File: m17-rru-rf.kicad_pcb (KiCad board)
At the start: 4 copper layers, 255 x 165 mm, 182 parts, among them J1 Conn_01x01_Pin, J2 Conn_Coaxial, J3 Conn_01x05, J4 Conn_01x05, J5 Conn_01x16, J6 Conn_Coaxial, Q1 BSS138, Q2 BSS138, Q3 NP100P04PDG, U1 LM317_SOT-223, U10 CC1200, U11 AD8318ACPZ-REEL7, U12 AD8318ACPZ-REEL7, U13 STM32F405RGTx, U2 LT1013DIDR, U3 TL431, U4 RA60H3847H1, U6 CC1200, X1 40MHz, Y1 12MHz

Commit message: LM317 protection diode location update
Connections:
- C3 pad 1: Net-(U1-ADJ) -> Net-(D2-A)
- D2 pad 2: GND -> Net-(D2-A)
- R6 pad 1: Net-(U1-ADJ) -> Net-(D2-A)
- R7 pad 2: Net-(U1-ADJ) -> Net-(D2-A)
- U1 pad 1: Net-(U1-ADJ) -> Net-(D2-A)
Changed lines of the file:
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@@
   (net 19 "Net-(U11-INHI)")
   (net 20 "Net-(R1-Pad2)")
-  (net 21 "Net-(U1-ADJ)")
+  (net 21 "Net-(D2-A)")
   (net 22 "Net-(U11-TADJ)")
   (net 23 "unconnected-(U11-TEMP-Pad13)")
@@
       (net 27 "Net-(R7-Pad1)") (pintype "passive"))
     (pad "2" smd roundrect (at 0.825 0) (size 0.8 0.95) (layers "F.Cu" "F.Paste" "F.Mask") (roundrect_rratio 0.25)
-      (net 21 "Net-(U1-ADJ)") (pintype "passive"))
+      (net 21 "Net-(D2-A)") (pintype "passive"))
     (model "${KICAD6_3DMODEL_DIR}/Resistor_SMD.3dshapes/R_0603_1608Metric.wrl"
       (offset (xyz 0 0 0))
@@
       (stroke (width 0.1) (type solid)) (layer "F.Fab"))
     (pad "1" smd roundrect (at -0.825 0) (size 0.8 0.95) (layers "F.Cu" "F.Paste" "F.Mask") (roundrect_rratio 0.25)
-      (net 21 "Net-(U1-ADJ)") (pintype "passive"))
+      (net 21 "Net-(D2-A)") (pintype "passive"))
     (pad "2" smd roundrect (at 0.825 0) (size 0.8 0.95) (layers "F.Cu" "F.Paste" "F.Mask") (roundrect_rratio 0.25)
       (net 24 "Net-(D1-A)") (pintype "passive"))
@@
       (stroke (width 0.1) (type solid)) (layer "F.Fab"))
     (pad "1" smd rect (at -3.15 -2.3) (size 2 1.5) (layers "F.Cu" "F.Paste" "F.Mask")
-      (net 21 "Net-(U1-ADJ)") (pinfunction "ADJ") (pintype "input"))
+      (net 21 "Net-(D2-A)") (pinfunction "ADJ") (pintype "input"))
     (pad "2" smd rect (at -3.15 0) (size 2 1.5) (layers "F.Cu" "F.Paste" "F.Mask")
       (net 24 "Net-(D1-A)") (pinfunction "VO") (pintype "power_out"))
@@
       (stroke (width 0.1) (type solid)) (layer "F.Fab"))
     (pad "1" smd roundrect (at -0.775 0) (size 0.9 0.95) (layers "F.Cu" "F.Paste" "F.Mask") (roundrect_rratio 0.25)
-      (net 21 "Net-(U1-ADJ)") (pintype "passive"))
+      (net 21 "Net-(D2-A)") (pintype "passive"))
     (pad "2" smd roundrect (at 0.775 0) (size 0.9 0.95) (layers "F.Cu" "F.Paste" "F.Mask") (roundrect_rratio 0.25)
       (net 9 "GND") (pintype "passive"))
@@
       (net 24 "Net-(D1-A)") (pinfunction "K") (pintype "passive"))
     (pad "2" smd roundrect (at 2 0) (size 2.5 1.8) (layers "F.Cu" "F.Paste" "F.Mask") (roundrect_rratio 0.1388888889)
-      (net 9 "GND") (pinfunction "A") (pintype "passive"))
+      (net 21 "Net-(D2-A)") (pinfunction "A") (pintype "passive"))
     (model "${KICAD6_3DMODEL_DIR}/Diode_SMD.3dshapes/D_SMA.wrl"
       (offset (xyz 0 0 0))

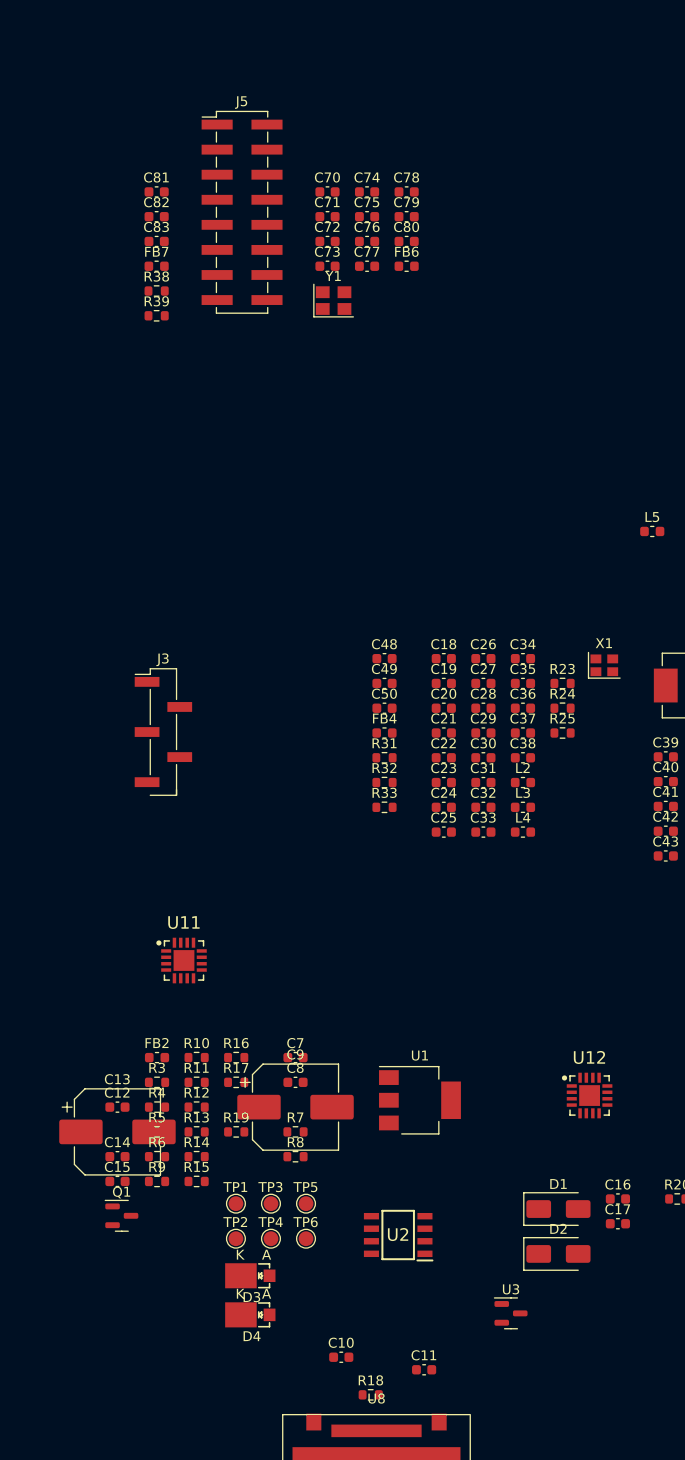
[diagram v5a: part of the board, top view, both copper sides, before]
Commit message: added missing 40MHz source
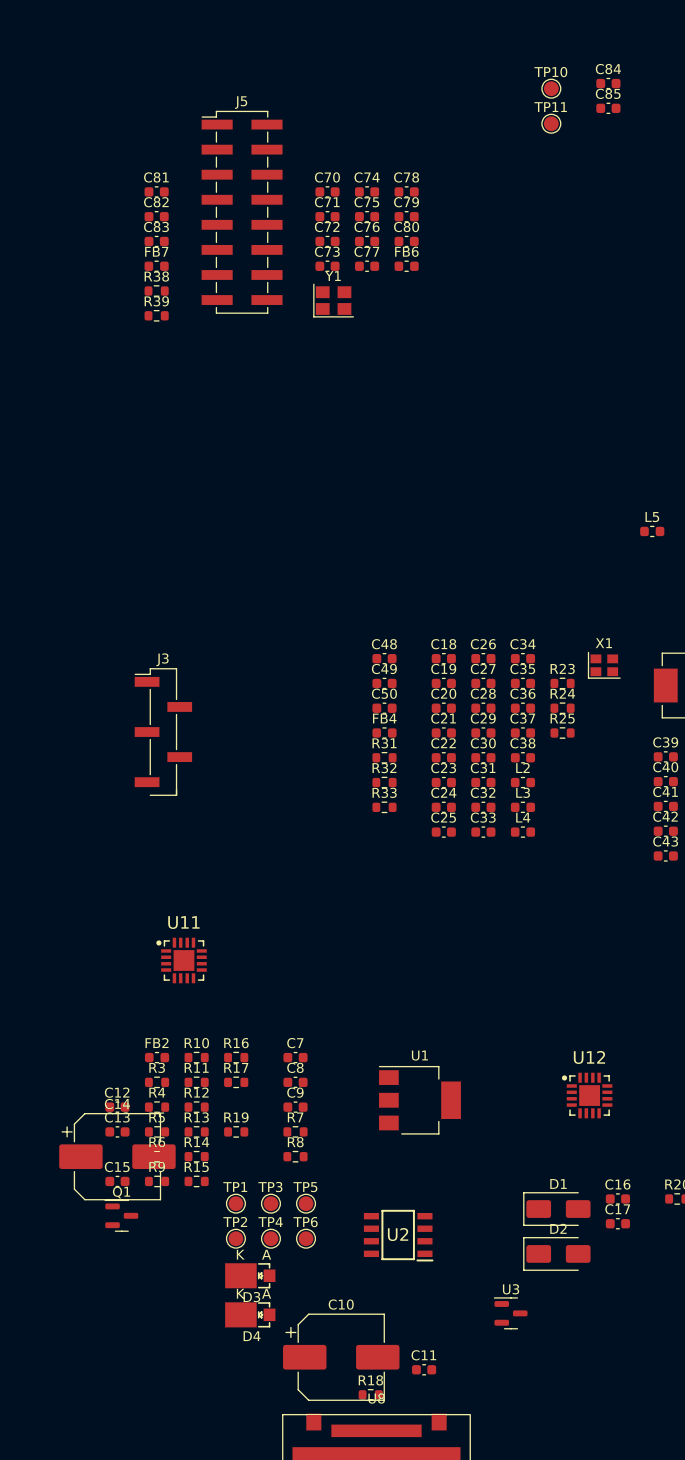
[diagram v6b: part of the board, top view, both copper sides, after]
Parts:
- added C84: 100n, Capacitor_SMD:C_0603_1608Metric, F.Cu at (149.2, 57.5)
- added C85: 1n, Capacitor_SMD:C_0603_1608Metric, F.Cu at (149.2, 60.0)
- added TP10: ~, TestPoint:TestPoint_Pad_D1.5mm, F.Cu at (143.4, 58.0)
- added TP11: ~, TestPoint:TestPoint_Pad_D1.5mm, F.Cu at (143.4, 61.6)
- C10, C14: value 22u/6.3V -> 100u/50V; footprint Capacitor_SMD:C_0603_1608Metric -> Capacitor_SMD:CP_Elec_8x10.5
- C11: value 100n -> 22u/6.3V
- C13, C9: value 100u/50V -> 100n; footprint Capacitor_SMD:CP_Elec_8x10.5 -> Capacitor_SMD:C_0603_1608Metric
- C15: value 47n -> 22u/6.3V
- C18: value 1n -> 47n
- C19, C44: value 47n -> 1n
- C20, C43: value 1n5 -> 47n
- C21, C45: value 47n -> 1n5
- C28, C50, C59: value 100n -> 47n
- C29: value 47n -> 100n
- C3: value 100n -> 3n9
- C32: value 39p -> 47n
- C33: value 56p -> 39p
- C34: value 2p2 -> 56p
- C35: value 10n -> 2p2
- C36: value 5p1 -> 10n
- C37: value 100p -> 5p1
- C38: value 6n2 -> 100p
- C39: value 47n -> 6n2
- C4, C81: value 1u -> 100n
- C49, C55: value 5p1 -> 47n
- C5, C73, C74: value 100n -> 1u
- C51, C54, C57: value 47n -> 5p1
- C52: value 5p1 -> 100n
- C56: value 6p2 -> 47n
- C58: value 1u -> 6p2
- C60, C83: value 1n -> 1u
- C63, C66, C7: value 1n -> 100n
- C64, C8: value 100n -> 1n
- C67, C68: value 10p -> 1n
- C69, C70: value 2u2 -> 10p
- C71, C72: value 1u -> 2u2
- C75, C76: value 10n -> 100n
- C77, C78: value 100n -> 10n
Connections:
- C10 pad 1: GND -> /RF PA/RF_PA_VDD
- C10 pad 2: /Power supply/13.8V_OUT -> GND
- C11 pad 1: /Power supply/13.8V_OUT -> GND
- C11 pad 2: GND -> /Power supply/13.8V_OUT
- C12 pad 1: Net-(U5-BST) -> /Power supply/13.8V_OUT
- C12 pad 2: Net-(U5-SW) -> GND
- C13 pad 1: /Power supply/13.8V_OUT -> Net-(U5-BST)
- C13 pad 2: GND -> Net-(U5-SW)
- C14 pad 1: GND -> /Power supply/13.8V_OUT
- C14 pad 2: /Exciter/3.3V_IN -> GND
- C15 pad 1: /Exciter/EXCITER_3V3 -> GND
- C15 pad 2: GND -> /Exciter/3.3V_IN
- C18 pad 1: Net-(X1-OUT) -> /Exciter/EXCITER_3V3
- C18 pad 2: Net-(U6-EXT_XOSC) -> GND
- C19 pad 1: /Exciter/EXCITER_3V3 -> /Exciter/40M_OUT
- C19 pad 2: GND -> Net-(U6-EXT_XOSC)
- C20 pad 1: Net-(U6-LPF0) -> /Exciter/EXCITER_3V3
- C20 pad 2: Net-(U6-LPF1) -> GND
- C21 pad 1: /Exciter/EXCITER_3V3 -> Net-(U6-LPF0)
- C21 pad 2: GND -> Net-(U6-LPF1)
- C27 pad 1: Net-(U6-DCPL_XOSC) -> /Exciter/EXCITER_3V3
- C28 pad 1: /Exciter/3.3V_IN -> Net-(U6-DCPL_XOSC)
- C29 pad 1: Net-(U6-DCPL_PFD_CHP) -> /Exciter/3.3V_IN
- C3 pad 1: Net-(D2-A) -> Net-(U2-2OUT)
- C3 pad 2: GND -> Net-(U2-2IN-)
- C30 pad 1: Net-(U6-DCPL_VCO) -> Net-(U6-DCPL_PFD_CHP)
- C31 pad 1: Net-(U6-DCPL) -> Net-(U6-DCPL_VCO)
- C32 pad 1: Net-(C32-Pad1) -> Net-(U6-DCPL)
- C32 pad 2: Net-(U6-PA) -> GND
- C33 pad 1: /Exciter/EXCITER_3V3 -> Net-(C33-Pad1)
- C33 pad 2: Net-(C33-Pad2) -> Net-(U6-PA)
- C34 pad 1: Net-(C34-Pad1) -> /Exciter/EXCITER_3V3
- C34 pad 2: Net-(C32-Pad1) -> Net-(C34-Pad2)
- C35 pad 1: /Exciter/EXCITER_3V3 -> Net-(C35-Pad1)
- C35 pad 2: GND -> Net-(C33-Pad1)
- C36 pad 1: Net-(C34-Pad1) -> /Exciter/EXCITER_3V3
- C37 pad 1: /Exciter/EXCITER_3V3 -> Net-(C35-Pad1)
- C38 pad 1: Net-(C38-Pad1) -> /Exciter/EXCITER_3V3
- C39 pad 1: /Receiver/RX_3V3 -> Net-(C39-Pad1)
- C4 pad 1: Net-(D1-A) -> Net-(D2-A)
- C43 pad 1: Net-(U10-LPF0) -> /Receiver/RX_3V3
- C43 pad 2: Net-(U10-LPF1) -> GND
- C44 pad 1: /Receiver/RX_3V3 -> Net-(U10-EXT_XOSC)
- C44 pad 2: GND -> /Exciter/40M_OUT
- C45 pad 1: /Receiver/RX_3V3 -> Net-(U10-LPF0)
- C45 pad 2: GND -> Net-(U10-LPF1)
- C49 pad 1: Net-(U10-LNA_P) -> /Receiver/RX_3V3
- C49 pad 2: Net-(C49-Pad2) -> GND
- C5 pad 1: /RF PA/RF_PA_1V1 -> Net-(D1-A)
- C50 pad 1: /Exciter/3.3V_IN -> /Receiver/RX_3V3
- C51 pad 1: Net-(U10-DCPL_XOSC) -> Net-(U10-LNA_P)
- C51 pad 2: GND -> Net-(C51-Pad2)
- C52 pad 1: Net-(U10-LNA_N) -> /Exciter/3.3V_IN
- C52 pad 2: Net-(C49-Pad2) -> GND
- C53 pad 1: Net-(U10-DCPL_PFD_CHP) -> Net-(U10-DCPL_XOSC)
- C54 pad 1: Net-(U10-DCPL_VCO) -> Net-(U10-LNA_N)
- C54 pad 2: GND -> Net-(C51-Pad2)
- C55 pad 1: Net-(C55-Pad1) -> Net-(U10-DCPL_PFD_CHP)
- C55 pad 2: Net-(C55-Pad2) -> GND
- C56 pad 1: Net-(C55-Pad2) -> Net-(U10-DCPL_VCO)
- C57 pad 1: Net-(U10-DCPL) -> Net-(C57-Pad1)
- C57 pad 2: GND -> Net-(C57-Pad2)
- C58 pad 1: /Exciter/3.3V_IN -> Net-(C57-Pad2)
- C59 pad 1: Net-(U11-CLPF) -> Net-(U10-DCPL)
- C6 pad 1: /RF PA/RF_PA_7V -> /RF PA/RF_PA_1V1
- C60 pad 1: GND -> /Exciter/3.3V_IN
- C60 pad 2: Net-(U11-INLO) -> GND
- C61 pad 1: /RF detectors/RF_DET_3V3 -> Net-(U11-CLPF)
- C62 pad 1: /RF coupler/FWD_RF -> GND
- C62 pad 2: Net-(U11-INHI) -> Net-(U11-INLO)
- C64 pad 1: Net-(U12-CLPF) -> /RF coupler/FWD_RF
- C64 pad 2: GND -> Net-(U11-INHI)
- C65 pad 1: GND -> /RF detectors/RF_DET_3V3
- C65 pad 2: Net-(U12-INLO) -> GND
- C66 pad 1: /RF coupler/REF_RF -> Net-(U12-CLPF)
- C66 pad 2: Net-(U12-INHI) -> GND
- C67 pad 1: /MCU/OSC1 -> GND
- C67 pad 2: GND -> Net-(U12-INLO)
- C68 pad 1: /MCU/OSC2 -> /RF coupler/REF_RF
- C68 pad 2: GND -> Net-(U12-INHI)
- C69 pad 1: Net-(U13-VCAP_1) -> /MCU/OSC1
- C70 pad 1: Net-(U13-VCAP_2) -> /MCU/OSC2
- C71 pad 1: /Exciter/3.3V_IN -> Net-(U13-VCAP_1)
- C72 pad 1: /Exciter/3.3V_IN -> Net-(U13-VCAP_2)
- C73 pad 1: /MCU/MCU_3V3 -> /Exciter/3.3V_IN
- C74 pad 1: /MCU/MCU_VDDA_3V3 -> /Exciter/3.3V_IN
- C78 pad 1: /MCU/MCU_3V3 -> /MCU/MCU_VDDA_3V3
- C8 pad 1: GND -> /RF PA/RF_PA_7V
- C8 pad 2: Net-(U3-K) -> GND
- C81 pad 1: /Exciter/3.3V_IN -> /MCU/MCU_3V3
- C82 pad 1: /Interface/INTERFACE_3V3 -> /MCU/MCU_3V3
- C83 pad 1: /Interface/INTERFACE_3V3 -> /Exciter/3.3V_IN
- C9 pad 1: /RF PA/RF_PA_VDD -> GND
- C9 pad 2: GND -> Net-(U3-K)
- L10 pad 2: Net-(C55-Pad2) -> Net-(C57-Pad2)
- L2 pad 1: Net-(C33-Pad2) -> Net-(C34-Pad2)
- L3 pad 1: Net-(C34-Pad1) -> Net-(C35-Pad1)
- L3 pad 2: Net-(C32-Pad1) -> Net-(C33-Pad1)
- L4 pad 1: Net-(C38-Pad1) -> Net-(C39-Pad1)
- L4 pad 2: Net-(C34-Pad1) -> Net-(C35-Pad1)
- L5 pad 2: Net-(C38-Pad1) -> Net-(C39-Pad1)
- L8 pad 2: Net-(C49-Pad2) -> Net-(C51-Pad2)
- L9 pad 1: Net-(C55-Pad1) -> Net-(C57-Pad1)
- L9 pad 2: Net-(C49-Pad2) -> Net-(C51-Pad2)
- R28 pad 1: Net-(C33-Pad2) -> Net-(C34-Pad2)
- TP1 pad 1: /RF PA/RF_PA_VGG -> /FWD_SENSE
- TP2 pad 1: /RF PA/RF_PA_1V1 -> Net-(R1-Pad2)
- TP3 pad 1: /RF PA/RF_PA_7V -> /RF PA/RF_PA_VGG
- TP4 pad 1: Net-(U3-K) -> /RF PA/RF_PA_1V1
- TP5 pad 1: Net-(Q1-G) -> /RF PA/RF_PA_7V
- TP6 pad 1: Net-(Q2-G) -> Net-(U3-K)
- TP7 pad 1: Net-(Q1-D) -> Net-(Q1-G)
- TP8 pad 1: /Power supply/13.8V_OUT -> Net-(Q2-G)
- TP9 pad 1: /Exciter/3.3V_IN -> Net-(Q1-D)
- U10 pad 32: unconnected-(U10-EXT_XOSC-Pad32) -> Net-(U10-EXT_XOSC)
- X1 pad 3: Net-(X1-OUT) -> /Exciter/40M_OUT

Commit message: date and labels update
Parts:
- added C86: 100n, Capacitor_SMD:C_0603_1608Metric, F.Cu at (286.2, 91.5)
- added C87: 1u, Capacitor_SMD:C_0603_1608Metric, F.Cu at (286.2, 65.3)
- added C88: 100n, Capacitor_SMD:C_0603_1608Metric, F.Cu at (286.2, 67.8)
- added C89: 1n, Capacitor_SMD:C_0603_1608Metric, F.Cu at (286.2, 70.3)
- added L11: 22n, Inductor_SMD:L_0603_1608Metric, F.Cu at (286.2, 96.0)
- added R44: 10k, Resistor_SMD:R_0603_1608Metric, F.Cu at (286.2, 72.9)
- added R45: 10k, Resistor_SMD:R_0603_1608Metric, F.Cu at (286.2, 75.4)
- added R46: 10k, Resistor_SMD:R_0603_1608Metric, F.Cu at (286.2, 77.9)
- added TP12: TP, TestPoint:TestPoint_Pad_D1.5mm, F.Cu at (286.0, 82.9)
- added TP13: TP, TestPoint:TestPoint_Pad_D1.5mm, F.Cu at (286.0, 86.5)
- added U15: WH3538X-1, Parts:CIRC_H08, F.Cu at (260.7, 84.6)
- C11: value 22u/6.3V -> 100u/50V; footprint Capacitor_SMD:C_0603_1608Metric -> Capacitor_SMD:CP_Elec_8x10.5
- C12: value 100n -> 100u/50V; footprint Capacitor_SMD:C_0603_1608Metric -> Capacitor_SMD:CP_Elec_8x10.5
- C14: value 100u/50V -> 100n; footprint Capacitor_SMD:CP_Elec_8x10.5 -> Capacitor_SMD:C_0603_1608Metric
- C15: value 22u/6.3V -> 100n
- C16, C56: value 47n -> 100n
- C17: value 47n -> 100u/50V; footprint Capacitor_SMD:C_0603_1608Metric -> Capacitor_SMD:CP_Elec_8x10.5
- C18: value 47n -> 22u/6.3V
- C19: value 1n -> 22u/6.3V
- C21, C45: value 1n5 -> 47n
- C23, C48: value 47n -> 9p1
- C25, C49: value 47n -> 1n5
- C29, C52: value 100n -> 47n
- C33: value 39p -> 100n
- C34: value 56p -> 47n
- C35: value 2p2 -> 10n
- C36: value 10n -> 220n
- C37: value 5p1 -> 39p
- C38: value 100p -> 56p
- C39: value 6n2 -> 2p2
- C40: value 47n -> 10n
- C41, C55: value 47n -> 5p1
- C42: value 47n -> 100p
- C43: value 47n -> 6p2
- C44: value 1n -> 47n
- C51, C54, C57: value 5p1 -> 47n
- C58: value 6p2 -> 5p1
- C60: value 1u -> 10n
- C61: value 100n -> 5p1
- C62: value 1n -> 6p2
- C63: value 100n -> 220n
- C64: value 1n -> 1u
- C65, C67, C85: value 1n -> 100n
- C66: value 100n -> 1n
- C69: value 10p -> 1n
- C70: value 10p -> 100n
- C71, C72: value 2u2 -> 1n
- C73, C74: value 1u -> 10p
- C75, C76: value 100n -> 2u2
- C77, C78: value 10n -> 1u
- C81, C82: value 100n -> 10n
- C83: value 1u -> 100n
- J1: value Conn_01x01_Pin -> 13.8V
- J3: value Conn_01x05 -> DBG_CONN
- J4: value Conn_01x05 -> SWD_CONN
- J5: value Conn_01x16 -> DA15_CONN
- JP1: value ~ -> JP
- L10: value 22n -> 15n
- L2: value 56n -> 10u; footprint Inductor_SMD:L_0603_1608Metric -> Inductor_SMD:L_Vishay_IHLP-2525
- L3: value 15n -> 56n
- L4: value 43n -> 15n
- L5: value 22n -> 43n
- L6: value 27n -> 22n
- L7: value 56n -> 27n
- L8: value 27n -> 56n
- L9: value 15n -> 27n
- R22: value 24k -> 100k
- R23: value 75k -> 24k
- R24: value 100R -> 24k
- R25: value 100R -> 75k
- R26: value 100R -> 126k
- R27, R32: value 56k -> 100R
- R28: value 18R -> 100R
- R30: value 100R -> 56k
- R31: value 100R -> 18R
- R33: value 52R3 -> 100R
- R34: value 499R -> 100R
- R35: value 52R3 -> 56k
- R36: value 499R -> 52R3
- R37, R39: value 100R -> 499R
- R38: value 100R -> 52R3
- R40: value ~ -> 100R; footprint Parts:HALF_FLANGE_DUMMY_LOAD -> Resistor_SMD:R_0603_1608Metric
- R41, R42: value 10k -> 100R
- R43: value 10k -> J100N50X4B; footprint Resistor_SMD:R_0603_1608Metric -> Parts:HALF_FLANGE_DUMMY_LOAD
- TP1, TP10, TP11, TP2, TP3, TP4, TP5, TP6, TP7, TP8, TP9: value ~ -> TP
- U1: value LM317_SOT-223 -> LT1013DIDR; footprint Package_TO_SOT_SMD:SOT-223-3_TabPin2 -> Mine:SOIC127P600X175-8N
- U10: value CC1200 -> GAT-30+; footprint Package_DFN_QFN:QFN-32-1EP_5x5mm_P0.5mm_EP3.45x3.45mm -> Parts:GAT-30_LAND
- U11: value AD8318ACPZ-REEL7 -> CC1200; footprint Mine:QFN65P400X400X100-17N -> Package_DFN_QFN:QFN-32-1EP_5x5mm_P0.5mm_EP3.45x3.45mm
- U12: value AD8318ACPZ-REEL7 -> AD8318
- U13: value STM32F405RGTx -> AD8318; footprint Package_QFP:LQFP-64_10x10mm_P0.5mm -> Mine:QFN65P400X400X100-17N
- U14: value ~ -> STM32F405RGT6; footprint Parts:CIRC_H08 -> Package_QFP:LQFP-64_10x10mm_P0.5mm
- U2: value LT1013DIDR -> LM317_SOT-223; footprint Mine:SOIC127P600X175-8N -> Package_TO_SOT_SMD:SOT-223-3_TabPin2
- U5: value ~ -> TP6841
- U6: value CC1200 -> TP6841; footprint Package_DFN_QFN:QFN-32-1EP_5x5mm_P0.5mm_EP3.45x3.45mm -> Package_TO_SOT_SMD:SOT-23-6
- U7: value ~ -> CC1200; footprint Parts:GAT-30_LAND -> Package_DFN_QFN:QFN-32-1EP_5x5mm_P0.5mm_EP3.45x3.45mm
- U8: value ~ -> GAT-30+; footprint Parts:SYBD-30_LAND -> Parts:GAT-30_LAND
- U9: value ~ -> SYBD-30-62HP+; footprint Parts:GAT-30_LAND -> Parts:SYBD-30_LAND
- moved U14 60.1 mm to (264.0, 149.0)
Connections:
- C11 pad 1: GND -> /Power supply/13.8V_OUT
- C11 pad 2: /Power supply/13.8V_OUT -> GND
- C13 pad 1: Net-(U5-BST) -> /Power supply/13.8V_OUT
- C13 pad 2: Net-(U5-SW) -> GND
- C15 pad 1: GND -> Net-(U5-BST)
- C15 pad 2: /Exciter/3.3V_IN -> Net-(U5-SW)
- C16 pad 1: /Exciter/EXCITER_3V3 -> Net-(U6-BST)
- C16 pad 2: GND -> Net-(U6-SW)
- C17 pad 1: /Exciter/EXCITER_3V3 -> /Power supply/13.8V_OUT
- C18 pad 1: /Exciter/EXCITER_3V3 -> GND
- C18 pad 2: GND -> /Exciter/3.3V_IN
- C19 pad 1: /Exciter/40M_OUT -> GND
- C19 pad 2: Net-(U6-EXT_XOSC) -> /Power supply/5V_OUT
- C2 pad 1: /RF PA/RF_PA_VGG -> Net-(U1-1OUT)
- C2 pad 2: Net-(U2-1IN-) -> Net-(U1-1IN-)
- C21 pad 1: Net-(U6-LPF0) -> /Exciter/EXCITER_3V3
- C21 pad 2: Net-(U6-LPF1) -> GND
- C23 pad 1: /Exciter/EXCITER_3V3 -> /Exciter/40M_OUT
- C23 pad 2: GND -> Net-(U7-EXT_XOSC)
- C25 pad 1: /Exciter/EXCITER_3V3 -> Net-(U7-LPF0)
- C25 pad 2: GND -> Net-(U7-LPF1)
- C28 pad 1: Net-(U6-DCPL_XOSC) -> /Exciter/EXCITER_3V3
- C29 pad 1: /Exciter/3.3V_IN -> /Exciter/EXCITER_3V3
- C3 pad 1: Net-(U2-2OUT) -> /RF PA/RF_PA_VGG
- C3 pad 2: Net-(U2-2IN-) -> Net-(U1-2IN-)
- C30 pad 1: Net-(U6-DCPL_PFD_CHP) -> /Exciter/EXCITER_3V3
- C31 pad 1: Net-(U6-DCPL_VCO) -> /Exciter/EXCITER_3V3
- C32 pad 1: Net-(U6-DCPL) -> Net-(U7-DCPL_XOSC)
- C33 pad 1: Net-(C33-Pad1) -> /Exciter/3.3V_IN
- C33 pad 2: Net-(U6-PA) -> GND
- C34 pad 1: /Exciter/EXCITER_3V3 -> Net-(U7-DCPL_PFD_CHP)
- C34 pad 2: Net-(C34-Pad2) -> GND
- C35 pad 1: Net-(C35-Pad1) -> Net-(U7-DCPL_VCO)
- C35 pad 2: Net-(C33-Pad1) -> GND
- C36 pad 1: /Exciter/EXCITER_3V3 -> Net-(U7-DCPL)
- C37 pad 1: Net-(C35-Pad1) -> Net-(C37-Pad1)
- C37 pad 2: GND -> Net-(U7-PA)
- C38 pad 2: GND -> Net-(C38-Pad2)
- C39 pad 2: GND -> Net-(C37-Pad1)
- C40 pad 1: /Receiver/RX_3V3 -> /Exciter/EXCITER_3V3
- C41 pad 1: /Receiver/RX_3V3 -> Net-(C39-Pad1)
- C42 pad 1: /Receiver/RX_3V3 -> /Exciter/EXCITER_3V3
- C43 pad 1: /Receiver/RX_3V3 -> Net-(C43-Pad1)
- C44 pad 1: Net-(U10-EXT_XOSC) -> /Receiver/RX_3V3
- C44 pad 2: /Exciter/40M_OUT -> GND
- C45 pad 1: Net-(U10-LPF0) -> /Receiver/RX_3V3
- C45 pad 2: Net-(U10-LPF1) -> GND
- C48 pad 1: /Receiver/RX_3V3 -> Net-(U11-EXT_XOSC)
- C48 pad 2: GND -> /Exciter/40M_OUT
- C49 pad 1: /Receiver/RX_3V3 -> Net-(U11-LPF0)
- C49 pad 2: GND -> Net-(U11-LPF1)
- C51 pad 1: Net-(U10-LNA_P) -> /Receiver/RX_3V3
- C51 pad 2: Net-(C51-Pad2) -> GND
- C52 pad 1: /Exciter/3.3V_IN -> /Receiver/RX_3V3
- C53 pad 1: Net-(U10-DCPL_XOSC) -> /Receiver/RX_3V3
- C54 pad 1: Net-(U10-LNA_N) -> /Receiver/RX_3V3
- C54 pad 2: Net-(C51-Pad2) -> GND
- C55 pad 1: Net-(U10-DCPL_PFD_CHP) -> Net-(U11-LNA_P)
- C55 pad 2: GND -> Net-(C55-Pad2)
- C56 pad 1: Net-(U10-DCPL_VCO) -> /Exciter/3.3V_IN
- C57 pad 1: Net-(C57-Pad1) -> Net-(U11-DCPL_XOSC)
- C57 pad 2: Net-(C57-Pad2) -> GND
- C58 pad 1: Net-(C57-Pad2) -> Net-(U11-LNA_N)
- C59 pad 1: Net-(U10-DCPL) -> Net-(U11-DCPL_PFD_CHP)
- C60 pad 1: /Exciter/3.3V_IN -> Net-(U11-DCPL_VCO)
- C61 pad 1: Net-(U11-CLPF) -> Net-(C61-Pad1)
- C61 pad 2: GND -> Net-(C61-Pad2)
- C62 pad 1: GND -> Net-(C61-Pad2)
- C62 pad 2: Net-(U11-INLO) -> GND
- C63 pad 1: /RF detectors/RF_DET_3V3 -> Net-(U11-DCPL)
- C64 pad 1: /RF coupler/FWD_RF -> /Power supply/5V_OUT
- C64 pad 2: Net-(U11-INHI) -> GND
- C65 pad 1: /RF detectors/RF_DET_3V3 -> Net-(U12-CLPF)
- C66 pad 1: Net-(U12-CLPF) -> GND
- C66 pad 2: GND -> Net-(U12-INLO)
- C67 pad 1: GND -> /RF detectors/RF_DET_5V
- C67 pad 2: Net-(U12-INLO) -> GND
- C68 pad 1: /RF coupler/REF_RF -> /RF coupler/FWD_RF
- C69 pad 1: /MCU/OSC1 -> /RF detectors/RF_DET_5V
- C70 pad 1: /MCU/OSC2 -> Net-(U13-CLPF)
- C71 pad 1: Net-(U13-VCAP_1) -> GND
- C71 pad 2: GND -> Net-(U13-INLO)
- C72 pad 1: Net-(U13-VCAP_2) -> /RF coupler/REF_RF
- C72 pad 2: GND -> Net-(U13-INHI)
- C73 pad 1: /Exciter/3.3V_IN -> /MCU/OSC1
- C74 pad 1: /Exciter/3.3V_IN -> /MCU/OSC2
- C75 pad 1: /MCU/MCU_3V3 -> Net-(U14-VCAP_1)
- C76 pad 1: /MCU/MCU_VDDA_3V3 -> Net-(U14-VCAP_2)
- C77 pad 1: /MCU/MCU_3V3 -> /Exciter/3.3V_IN
- C78 pad 1: /MCU/MCU_VDDA_3V3 -> /Exciter/3.3V_IN
- C80 pad 1: /MCU/MCU_3V3 -> /MCU/MCU_VDDA_3V3
- C82 pad 1: /MCU/MCU_3V3 -> /MCU/MCU_VDDA_3V3
- C83 pad 1: /Exciter/3.3V_IN -> /MCU/MCU_3V3
- C84 pad 1: /Interface/INTERFACE_3V3 -> /MCU/MCU_3V3
- C85 pad 1: /Interface/INTERFACE_3V3 -> /MCU/MCU_3V3
- FB4 pad 1: /Exciter/3.3V_IN -> /Power supply/5V_OUT
- FB4 pad 2: /RF detectors/RF_DET_3V3 -> /RF detectors/RF_DET_5V
- L10 pad 1: /RF input filter/RF_OUT -> Net-(C61-Pad1)
- L10 pad 2: Net-(C57-Pad2) -> Net-(C55-Pad2)
- L2 pad 1: Net-(C34-Pad2) -> Net-(U6-SW)
- L2 pad 2: Net-(U6-PA) -> /Power supply/5V_OUT
- L3 pad 1: Net-(C35-Pad1) -> Net-(C38-Pad2)
- L3 pad 2: Net-(C33-Pad1) -> Net-(U7-PA)
- L4 pad 2: Net-(C35-Pad1) -> Net-(C37-Pad1)
- L5 pad 1: /Exciter/RF_OUT -> Net-(C43-Pad1)
- L6 pad 1: Net-(U10-LNA_P) -> /Exciter/RF_OUT
- L6 pad 2: GND -> Net-(C43-Pad1)
- L7 pad 1: Net-(U10-LNA_N) -> Net-(U11-LNA_P)
- L7 pad 2: Net-(U10-LNA_P) -> GND
- L8 pad 1: Net-(U10-LNA_N) -> Net-(U11-LNA_N)
- L8 pad 2: Net-(C51-Pad2) -> Net-(U11-LNA_P)
- L9 pad 1: Net-(C57-Pad1) -> Net-(U11-LNA_N)
- L9 pad 2: Net-(C51-Pad2) -> Net-(C55-Pad2)
- R10 pad 1: Net-(U2-2IN-) -> Net-(U1-2IN-)
- R10 pad 2: /RF PA/RF_PA_VGG -> Net-(U1-1OUT)
- R11 pad 1: Net-(U2-2IN-) -> Net-(U1-2IN-)
- R11 pad 2: Net-(U2-2OUT) -> /RF PA/RF_PA_VGG
- R22 pad 1: Net-(U5-FB) -> /Power supply/13.8V_OUT
- R22 pad 2: GND -> Net-(U6-EN)
- R23 pad 2: /Exciter/3.3V_IN -> GND
- R24 pad 1: Net-(U6-SCLK) -> Net-(U6-FB)
- R24 pad 2: /SPI_SCK -> GND
- R25 pad 1: Net-(U6-SI) -> Net-(U5-FB)
- R25 pad 2: /SPI_MOSI -> /Exciter/3.3V_IN
- R26 pad 1: Net-(U6-SO(GPIO1)) -> Net-(U6-FB)
- R26 pad 2: /SPI_MISO -> /Power supply/5V_OUT
- R27 pad 1: Net-(U6-RBIAS) -> Net-(U7-SCLK)
- R27 pad 2: GND -> /SPI_SCK
- R28 pad 1: Net-(C34-Pad2) -> Net-(U7-SI)
- R28 pad 2: /Exciter/EXCITER_3V3 -> /SPI_MOSI
- R29 pad 1: Net-(U10-SCLK) -> Net-(U7-SO(GPIO1))
- R29 pad 2: /SPI_SCK -> /SPI_MISO
- R3 pad 2: Net-(U2-1IN-) -> Net-(U1-1IN-)
- R30 pad 1: Net-(U10-SI) -> Net-(U7-RBIAS)
- R30 pad 2: /SPI_MOSI -> GND
- R31 pad 1: Net-(U10-SO(GPIO1)) -> Net-(C38-Pad2)
- R31 pad 2: /SPI_MISO -> /Exciter/EXCITER_3V3
- R32 pad 1: Net-(U10-RBIAS) -> Net-(U11-SCLK)
- R32 pad 2: GND -> /SPI_SCK
- R33 pad 1: GND -> Net-(U11-SI)
- R33 pad 2: /RF coupler/FWD_RF -> /SPI_MOSI
- R34 pad 1: Net-(U11-TADJ) -> Net-(U11-SO(GPIO1))
- R34 pad 2: GND -> /SPI_MISO
- R35 pad 1: GND -> Net-(U11-RBIAS)
- R35 pad 2: /RF coupler/REF_RF -> GND
- R36 pad 1: Net-(U12-TADJ) -> GND
- R36 pad 2: GND -> /RF coupler/FWD_RF
- R37 pad 1: Net-(U13-PB3) -> Net-(U12-TADJ)
- R37 pad 2: /SPI_SCK -> GND
- R38 pad 1: Net-(U13-PB4) -> GND
- R38 pad 2: /SPI_MISO -> /RF coupler/REF_RF
- R39 pad 1: Net-(U13-PB5) -> Net-(U13-TADJ)
- R39 pad 2: /SPI_MOSI -> GND
- R4 pad 2: Net-(U2-2IN+) -> Net-(U1-2IN+)
- R40 pad 1: Net-(R40-In) -> Net-(U14-PB3)
- R41 pad 1: /nRST -> Net-(U14-PB4)
- R41 pad 2: GND -> /SPI_MISO
- R42 pad 1: /TX_nCS -> Net-(U14-PB5)
- R42 pad 2: /Interface/INTERFACE_3V3 -> /SPI_MOSI
- R43 pad 1: /RX_nCS -> Net-(R43-In)
- R5 pad 2: Net-(U2-2IN+) -> Net-(U1-2IN+)
- R9 pad 1: /RF PA/RF_PA_VGG -> Net-(U1-1OUT)
- R9 pad 2: Net-(U2-1IN-) -> Net-(U1-1IN-)
- TP10 pad 1: /Power supply/13.8V_OUT -> Net-(Q1-D)
- TP11 pad 1: /Exciter/3.3V_IN -> /Power supply/13.8V_OUT
- TP4 pad 1: /RF PA/RF_PA_1V1 -> Net-(U1-1OUT)
- TP5 pad 1: /RF PA/RF_PA_7V -> /RF PA/RF_PA_1V1
- TP6 pad 1: Net-(U3-K) -> /RF PA/RF_PA_7V
- TP7 pad 1: Net-(Q1-G) -> Net-(U3-K)
- TP8 pad 1: Net-(Q2-G) -> Net-(Q1-G)
- TP9 pad 1: Net-(Q1-D) -> Net-(Q2-G)
- U1 pad 1: Net-(D2-A) -> /RF PA/RF_PA_1V1
- U1 pad 2: Net-(D1-A) -> GND
- U1 pad 3: /Power supply/13.8V_OUT -> Net-(U1-2IN+)
- U10 pad 1: /Receiver/RX_3V3 -> Net-(U10-In)
- U10 pad 2: /nRST -> GND
- U10 pad 3: unconnected-(U10-GPIO3-Pad3) -> /RF coupler/FWD_RF
- U10 pad 4: unconnected-(U10-GPIO2-Pad4) -> GND
- U11 pad 1: GND -> /Receiver/RX_3V3
- U11 pad 10: Net-(U11-TADJ) -> unconnected-(U11-GPIO0-Pad10)
- U11 pad 11: GND -> /RX_nCS
- U11 pad 12: GND -> /Receiver/RX_3V3
- U11 pad 13: unconnected-(U11-TEMP-Pad13) -> /Receiver/RX_3V3
- U11 pad 14: Net-(U11-INHI) -> Net-(U11-RBIAS)
- U11 pad 15: Net-(U11-INLO) -> /Receiver/RX_3V3
- U11 pad 16: /RF detectors/RF_DET_3V3 -> (no net)
- U11 pad 17: GND -> Net-(JP1-B)
- U11 pad 2: GND -> /nRST
- U11 pad 3: /RF detectors/RF_DET_3V3 -> unconnected-(U11-GPIO3-Pad3)
- U11 pad 4: /RF detectors/RF_DET_3V3 -> unconnected-(U11-GPIO2-Pad4)
- U11 pad 5: Net-(U11-CLPF) -> /Receiver/RX_3V3
- U11 pad 6: /FWD_SENSE -> Net-(U11-DCPL)
- U11 pad 7: /FWD_SENSE -> Net-(U11-SI)
- U11 pad 8: GND -> Net-(U11-SCLK)
- U11 pad 9: /RF detectors/RF_DET_3V3 -> Net-(U11-SO(GPIO1))
- U12 pad 16: /RF detectors/RF_DET_3V3 -> /RF detectors/RF_DET_5V
- U12 pad 3: /RF detectors/RF_DET_3V3 -> /RF detectors/RF_DET_5V
- U12 pad 4: /RF detectors/RF_DET_3V3 -> /RF detectors/RF_DET_5V
- U12 pad 6: /REF_SENSE -> /FWD_SENSE
- U12 pad 7: /REF_SENSE -> /FWD_SENSE
- U12 pad 9: /RF detectors/RF_DET_3V3 -> /RF detectors/RF_DET_5V
- U13 pad 1: /MCU/MCU_3V3 -> GND
- U13 pad 10: unconnected-(U13-PC2-Pad10) -> Net-(U13-TADJ)
- U13 pad 11: unconnected-(U13-PC3-Pad11) -> GND
- U13 pad 13: /MCU/MCU_VDDA_3V3 -> unconnected-(U13-TEMP-Pad13)
- U13 pad 14: /FWD_SENSE -> Net-(U13-INHI)
- U13 pad 15: /REF_SENSE -> Net-(U13-INLO)
- U13 pad 16: /MCU/AIN2 -> /RF detectors/RF_DET_5V
- U13 pad 17: /MCU/AIN3 -> GND
- U13 pad 2: unconnected-(U13-PC13-Pad2) -> GND
- U13 pad 3: unconnected-(U13-PC14-Pad3) -> /RF detectors/RF_DET_5V
- U13 pad 4: unconnected-(U13-PC15-Pad4) -> /RF detectors/RF_DET_5V
- U13 pad 5: /MCU/OSC1 -> Net-(U13-CLPF)
- U13 pad 6: /MCU/OSC2 -> /REF_SENSE
- U13 pad 7: /nRST -> /REF_SENSE
- U13 pad 8: unconnected-(U13-PC0-Pad8) -> GND
- U13 pad 9: unconnected-(U13-PC1-Pad9) -> /RF detectors/RF_DET_5V
- U14 pad 1: /Circulator/RF_IN -> /MCU/MCU_3V3
- U14 pad 2: /Circulator/RF_OUT -> unconnected-(U14-PC13-Pad2)
- U14 pad 3: Net-(R40-In) -> unconnected-(U14-PC14-Pad3)
- U2 pad 1: /RF PA/RF_PA_1V1 -> Net-(D2-A)
- U2 pad 2: GND -> Net-(D1-A)
- U2 pad 3: Net-(U2-2IN+) -> /Power supply/13.8V_OUT
- U6 pad 1: /Exciter/EXCITER_3V3 -> Net-(U6-BST)
- U6 pad 2: /nRST -> GND
- U6 pad 3: unconnected-(U6-GPIO3-Pad3) -> Net-(U6-FB)
- U6 pad 4: unconnected-(U6-GPIO2-Pad4) -> Net-(U6-EN)
- U6 pad 5: /Exciter/EXCITER_3V3 -> /Power supply/13.8V_OUT
- U6 pad 6: Net-(U6-DCPL) -> Net-(U6-SW)
- U7 pad 1: Net-(U7-In) -> /Exciter/EXCITER_3V3
- U7 pad 2: GND -> /nRST
- U7 pad 3: /RF coupler/REF_RF -> unconnected-(U7-GPIO3-Pad3)
- U7 pad 4: GND -> unconnected-(U7-GPIO2-Pad4)
- U8 pad 1: Net-(J2-In) -> Net-(U8-In)
- U8 pad 2: /Circulator/RF_OUT -> GND
- U8 pad 3: Net-(U8-Rev) -> /RF coupler/REF_RF
- U8 pad 4: Net-(U7-In) -> GND
- U9 pad 1: Net-(U8-Rev) -> Net-(J2-In)
- U9 pad 2: GND -> /Circulator/RF_OUT
- U9 pad 3: /RF coupler/FWD_RF -> Net-(U10-In)
- U9 pad 4: GND -> Net-(U8-In)
